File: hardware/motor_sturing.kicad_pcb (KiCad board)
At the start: 4 copper layers, 160 x 100 mm, 330 parts, among them CON1 BARREL_JACK, J1 DB25_STACKED, J2 ETHERNET_DUAL, M1 NMOS, M10 NMOS, M11 NMOS, M12 NMOS, M2 NMOS, M3 NMOS, M4 NMOS, M5 NMOS, M6 NMOS, M7 NMOS, M8 NMOS, M9 NMOS, P1 CONN_01X03, P11 CONN_01X01, P12 CONN_01X01, P13 CONN_01X01, P14 CONN_01X01, P15 CONN_01X01, P16 CONN_01X01, P17 CONN_01X01, P18 CONN_01X01, P19 CONN_01X01, P2 CONN_01X03, P20 CONN_01X01, P21 CONN_01X01, P22 CONN_01X01, P23 CONN_01X01, P24 CONN_01X01, P25 CONN_01X01, P3 CONN_01X03, P4 CONN_01X03, P5 CONN_02X07, P6 CONN_01X01, P7 CONN_01X01, P8 CONN_01X01, U1 LTC2351-14, U10 MAX3463, U11 MAX3463, U12 MAX3463, U13 MAX3463, U14 MAX3463, U15 ADuM3223BRZ, U16 TS321, U17 ACS758, U18 ADuM3223BRZ, U19 AD8226, U2 XC6SLXN-TQG144, U20 AD8226, U21 AD8226, U22 LTC2351-14, U23 LT3010, U24 ACS758, U25 AMC1204, U26 OKR_T3, U27 ADuM3223BRZ, U28 ACS758, U29 MAX3463, U3 W25Q80DV, U30 MAX3463, U31 MAX3463, U32 MAX3463, U33 MAX3463, U34 ADuM3223BRZ, U35 ACS758, U36 ADuM3223BRZ, U37 TS321, U38 AD8226, U39 AD8226, U4 KSZ9031RNXCA, U40 AD8226, U41 OKR_T3, U42 LT3010, U43 ACS758, U44 AMC1204, U45 OKR_T3, U46 TS321, U47 TS321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

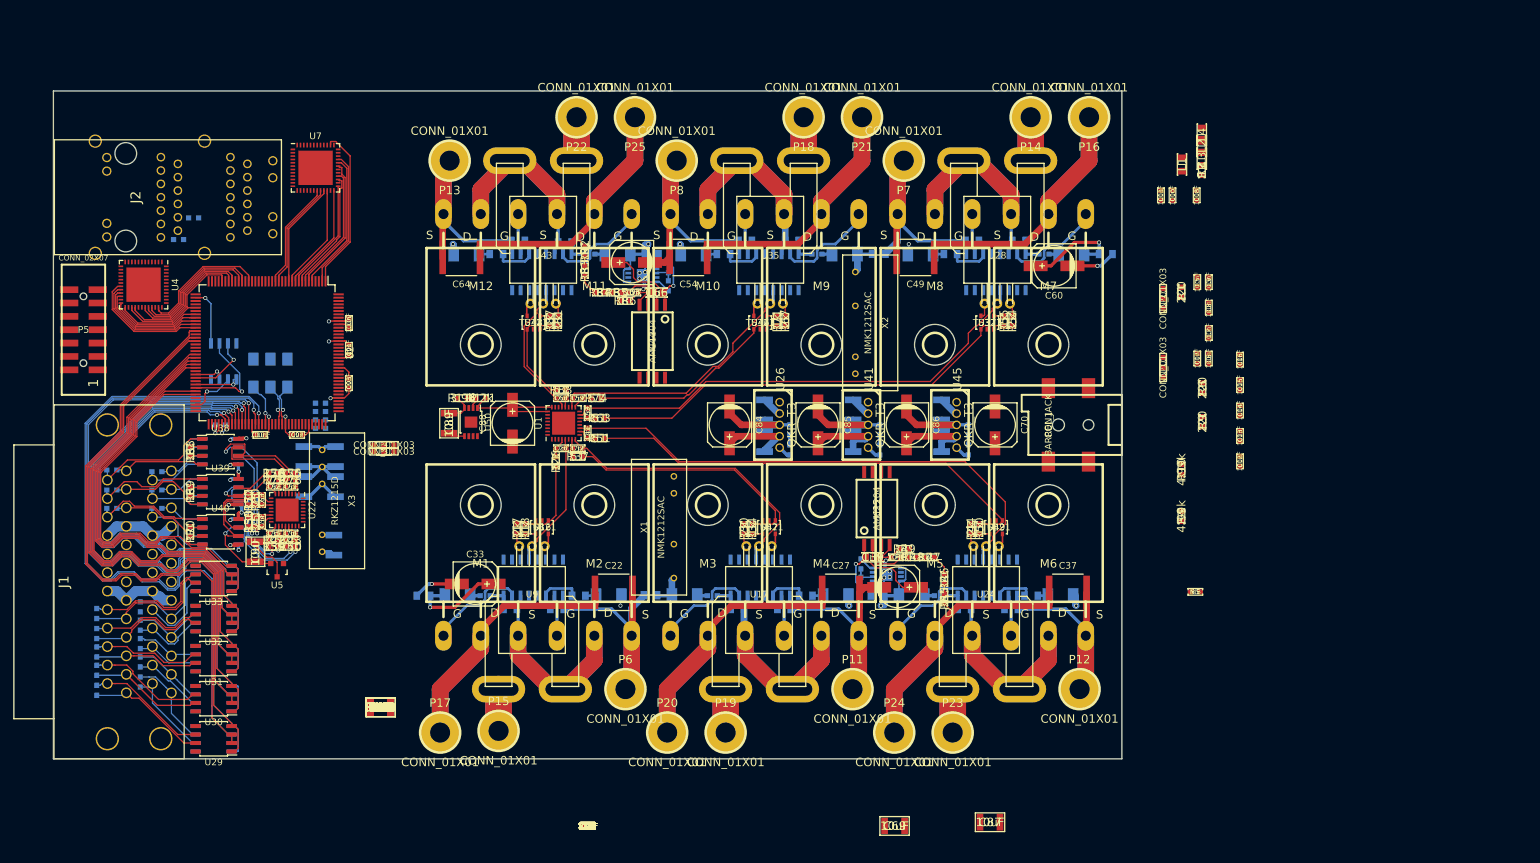
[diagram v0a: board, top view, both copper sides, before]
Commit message: Backup, clearing bottom of power section.
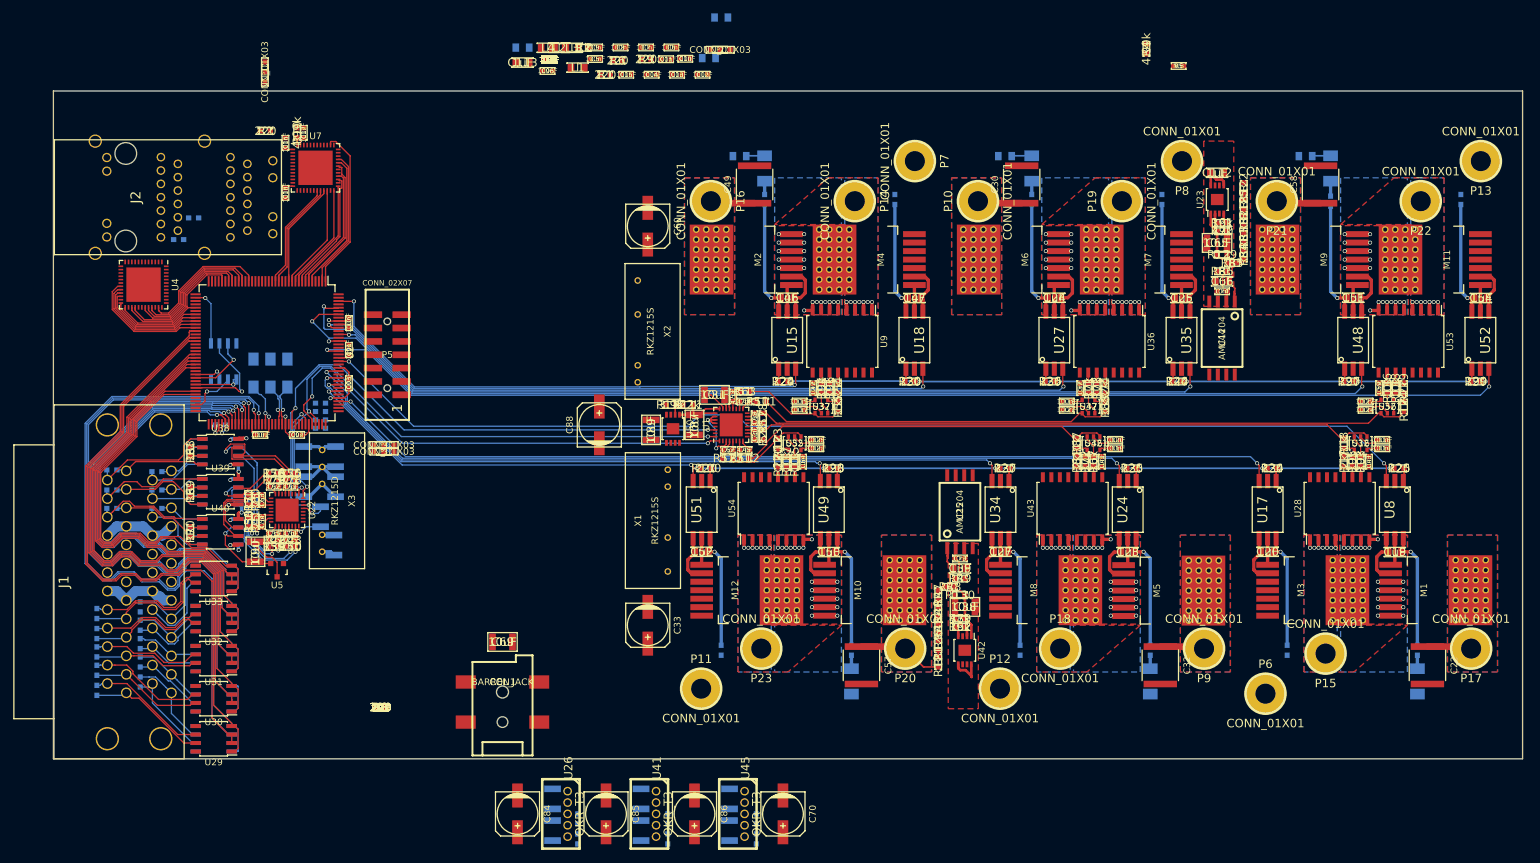
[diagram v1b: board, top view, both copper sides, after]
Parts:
- removed D11, D12, D2, D5, D6, D8: S1M, 00_Passives:DO-214AC(SMA)
- removed P24, P25: CONN_01X01, 00_Passives:conn_01x01_3mm
- added C112: 1uF, 00_Local:C0805, F.Cu at (204.2, 62.2)
- added C113: 1uF, 00_Local:C0805, F.Cu at (100.2, 45.8)
- added C114: 100nF, 00_Passives:C0603, F.Cu at (229.0, 103.5)
- added C115: 100nF, 00_Passives:C0603, F.Cu at (141.8, 96.5)
- added C116: 100nF, 00_Passives:C0603, F.Cu at (229.0, 102.2)
- added C117: 100nF, 00_Passives:C0603, F.Cu at (141.8, 97.8)
- added C118: 100nF, 00_Passives:C0603, F.Cu at (181.8, 96.5)
- added C119: 100nF, 00_Passives:C0603, F.Cu at (189.0, 103.5)
- added C120: 100nF, 00_Passives:C0603, F.Cu at (189.0, 102.2)
- added C121: 100nF, 00_Passives:C0603, F.Cu at (181.8, 97.8)
- added C122: 100nF, 00_Passives:C0603, F.Cu at (226.5, 96.5)
- added C123: 100nF, 00_Passives:C0603, F.Cu at (144.2, 103.5)
- added C124: 100nF, 00_Passives:C0603, F.Cu at (226.5, 97.8)
- added C125: 100nF, 00_Passives:C0603, F.Cu at (144.2, 102.2)
- added P10: CONN_01X01, 00_Passives:conn_01x01_3mm, F.Cu at (168.4, 66.5)
- added P9: CONN_01X01, 00_Passives:conn_01x01_3mm, F.Cu at (202.3, 133.5)
- added R113: 22, 00_Local:R0603, B.Cu at (130.0, 133.8)
- added R114: 22, 00_Local:R0603, B.Cu at (240.8, 66.3)
- added R115: 10k, 00_Passives:R0603, F.Cu at (141.0, 105.5)
- added R116: 10k, 00_Passives:R0603, F.Cu at (229.8, 94.5)
- added R117: 10k, 00_Passives:R0603, F.Cu at (139.8, 105.5)
- added R118: 10k, 00_Passives:R0603, F.Cu at (231.0, 94.5)
- added R119: 2k, 00_Local:R0603, F.Cu at (232.2, 94.5)
- added R120: 2k, 00_Local:R0603, F.Cu at (138.5, 105.5)
- added R121: R, 00_Local:R0603, F.Cu at (162.5, 135.5)
- added R122: R, 00_Local:R0603, F.Cu at (208.2, 64.5)
- added R123: 1k, 00_Local:R0603, F.Cu at (138.5, 102.8)
- added R124: 1k, 00_Local:R0603, F.Cu at (232.2, 97.2)
- added R125: R, 00_Local:R0603, F.Cu at (208.2, 67.0)
- added R126: R, 00_Local:R0603, F.Cu at (162.5, 133.0)
- added R127: 51, 00_Local:R0603, F.Cu at (131.0, 105.0)
- added R128: 51, 00_Local:R0603, F.Cu at (136.2, 99.0)
- added R129: 0.1, 00_Local:R0603, F.Cu at (205.0, 74.5)
- added R130: 0.1, 00_Local:R0603, F.Cu at (165.8, 125.5)
- added U51: Si8261BCD-C-IS, 00_Passives:SOIC-6_6.8x4.6mm_Pitch1.27mm, F.Cu at (127.1, 112.7)
- added U52: Si8261BCD-C-IS, 00_Passives:SOIC-6_6.8x4.6mm_Pitch1.27mm, F.Cu at (243.7, 87.3)
- added U53: ACS722KMATR-20AB-T, Housings_SOIC:SOIC-16_7.5x10.3mm_Pitch1.27mm, F.Cu at (232.9, 87.5)
- added U54: ACS722KMATR-20AB-T, Housings_SOIC:SOIC-16_7.5x10.3mm_Pitch1.27mm, F.Cu at (137.9, 112.5)
- added U55: TS321, 00_Passives:SOT23_5, F.Cu at (141.0, 102.7)
- added U56: TS321, 00_Passives:SOT23_5, F.Cu at (229.8, 97.2)
- C19, C20, C23, C24, C25, C46, C47, C50, C51, C52, R89, R90, R91, R92, U23, U42: moved to F.Cu
- C27, C54: value 1uF/630V -> 1uF; footprint Capacitors_SMD:C_2220 -> 00_Local:C0805
- C30, C57: value 1uF -> 1uF/630V; footprint 00_Local:C0805 -> Capacitors_SMD:C_2220; moved to F.Cu
- C32: value 47pF -> 1uF/630V; footprint 00_Local:C0603 -> Capacitors_SMD:C_2220
- C37, C64: value 1uF/630V -> 10nF; footprint Capacitors_SMD:C_2220 -> 00_Passives:C0603
- C38, C65: value 100uF/16V -> 10uF; footprint Capacitors_SMD:c_elec_6.3x5.3 -> 00_Passives:C1210
- C40: moved to B.Cu
- C41, C59: value 47pF -> 10nF; footprint 00_Local:C0603 -> 00_Passives:C0603
- C44, C45, C67: value 10nF -> 47pF; footprint 00_Passives:C0603 -> 00_Local:C0603
- C58: value 10nF -> 1uF/630V; footprint 00_Passives:C0603 -> Capacitors_SMD:C_2220
- M1, M10, M11, M12, M2, M3, M4, M5, M6, M7, M8, M9: value NMOS -> C3M0280090J; footprint 00_Passives:TO-247_GDS_below_board -> 00_Passives:TO-263-7-GDSKS
- R100, R97, R98, R99: value 10k -> 220
- R101, R102: value 10k -> 51; footprint 00_Passives:R0603 -> 00_Local:R0603
- R103, R104: value 10k -> 22; footprint 00_Passives:R0603 -> 00_Local:R0603; moved to B.Cu
- R16, R53, R62: footprint 00_Local:R0805 -> 00_Local:R0603
- R24, R35: value 22 -> 220; footprint 00_Local:R0603 -> 00_Passives:R0603; moved to F.Cu
- R25, R36: value 22 -> 220; footprint 00_Local:R0805 -> 00_Passives:R0603; moved to F.Cu
- R30, R44: value 2k -> 220; footprint 00_Local:R0603 -> 00_Passives:R0603
- R34: value 1k -> 220; footprint 00_Local:R0603 -> 00_Passives:R0603
- R37: value 51 -> 220; footprint 00_Local:R0603 -> 00_Passives:R0603
- R50: value 1k -> 22; moved to B.Cu
- R51: value 51 -> 22; moved to B.Cu
- R67: value 2k -> 10k; footprint 00_Local:R0603 -> 00_Passives:R0603
- R71: value 1k -> 10k; footprint 00_Local:R0603 -> 00_Passives:R0603
- R72: value 22 -> 10k; footprint 00_Local:R0603 -> 00_Passives:R0603; moved to F.Cu
- R73: value 22 -> 10k; footprint 00_Local:R0805 -> 00_Passives:R0603; moved to F.Cu
- R74: value 51 -> 2k
- R88: value 51 -> 1k
- U15, U18, U27, U34, U8: value ADuM3223BRZ -> Si8261BCD-C-IS; footprint Housings_SOIC:SOIC-16_3.9x9.9mm_Pitch1.27mm -> 00_Passives:SOIC-6_6.8x4.6mm_Pitch1.27mm; moved to F.Cu
- U17, U24, U35: value ACS758 -> Si8261BCD-C-IS; footprint 00_Passives:acs758 -> 00_Passives:SOIC-6_6.8x4.6mm_Pitch1.27mm
- U28, U43, U9: value ACS758 -> ACS722KMATR-20AB-T; footprint 00_Passives:acs758 -> Housings_SOIC:SOIC-16_7.5x10.3mm_Pitch1.27mm
- U36: value ADuM3223BRZ -> ACS722KMATR-20AB-T; footprint Housings_SOIC:SOIC-16_3.9x9.9mm_Pitch1.27mm -> Housings_SOIC:SOIC-16_7.5x10.3mm_Pitch1.27mm; moved to F.Cu
- U48, U49: value TS321 -> Si8261BCD-C-IS; footprint 00_Passives:SOT23_5 -> 00_Passives:SOIC-6_6.8x4.6mm_Pitch1.27mm
- X1, X2: value NMK1212SAC -> RKZ1215S
- moved R99 171.1 mm to (243.0, 93.5)
- moved R104 161.2 mm to (221.2, 66.5), turned to 90 degrees
- moved C58 161.1 mm to (219.8, 64.0), turned to 90 degrees
- moved P17 154.9 mm to (242.3, 133.5), turned to 180 degrees
- moved P13 154.4 mm to (243.8, 60.5)
- moved R97 153.0 mm to (224.0, 93.5)
- moved C43 152.5 mm to (227.0, 105.5), turned to 270 degrees
- moved R93 151.3 mm to (225.8, 105.5), turned to 90 degrees
- moved R95 150.1 mm to (224.5, 105.5), turned to 270 degrees
- moved C16 146.6 mm to (64.8, 57.7)
- moved D1 144.3 mm to (234.2, 138.4), turned to 90 degrees
- moved R10 141.7 mm to (66.5, 56.2)
- moved P1 141.6 mm to (61.7, 47.2)
- moved R15 139.8 mm to (234.2, 133.7), turned to 270 degrees
- moved C17 138.0 mm to (67.5, 56.2)
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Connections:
- net Net-(C22-Pad1) renamed /Drive_1/HV0
- net Net-(U2-Pad97) renamed /FPGA/HB_DISABLE
- C20 pad 2: /Drive_1/BRIDGE- -> Net-(C20-Pad2)
- C21 pad 1: /Drive_1/ISOL_12V -> /Drive_1/ISOL_15V
- C23 pad 1: /Drive_1/ISOL_12V -> Net-(C23-Pad1)
- C23 pad 2: /Drive_1/BRIDGE- -> Net-(C23-Pad2)
- C25 pad 2: /Drive_1/BRIDGE- -> Net-(C25-Pad2)
- C27 pad 2: /Drive_1/BRIDGE- -> Net-(C27-Pad2)
- C28 pad 1: /Drive_1/ISOL_12V -> /Drive_1/ISOL_15V
- C29 pad 1: Net-(C29-Pad1) -> /Drive_2/ISOL_15V
- C29 pad 2: Net-(C29-Pad2) -> /Drive_2/BRIDGE-
- C30 pad 1: Net-(C30-Pad1) -> /Drive_2/HV1
- C30 pad 2: /Drive_1/BRIDGE- -> /Drive_2/BRIDGE-
- C32 pad 1: /Drive_1/CUR1 -> /Drive_1/HV1
- C32 pad 2: GND -> /Drive_1/BRIDGE-
- C33 pad 1: /Drive_1/ISOL_12V -> /Drive_1/ISOL_15V
- C37 pad 2: /Drive_1/BRIDGE- -> GND
- C38 pad 1: /Drive_1/ISOL_5V -> Net-(C38-Pad1)
- C41 pad 1: /Drive_1/CUR2 -> Net-(C41-Pad1)
- C44 pad 1: Net-(C44-Pad1) -> /Drive_2/CUR1
- C45 pad 1: Net-(C45-Pad1) -> /Drive_1/CUR1
- C47 pad 2: /Drive_2/BRIDGE- -> Net-(C47-Pad2)
- C48 pad 1: /Drive_2/ISOL_12V -> /Drive_2/ISOL_15V
- C49 pad 1: Net-(C49-Pad1) -> /Drive_2/HV0
- C50 pad 1: /Drive_2/ISOL_12V -> Net-(C50-Pad1)
- C50 pad 2: /Drive_2/BRIDGE- -> Net-(C50-Pad2)
- C52 pad 2: /Drive_2/BRIDGE- -> Net-(C52-Pad2)
- C54 pad 2: /Drive_2/BRIDGE- -> Net-(C54-Pad2)
- C55 pad 1: /Drive_2/ISOL_12V -> /Drive_2/ISOL_15V
- C56 pad 1: Net-(C56-Pad1) -> /Drive_1/ISOL_15V
- C56 pad 2: Net-(C56-Pad2) -> /Drive_1/BRIDGE-
- C57 pad 1: Net-(C57-Pad1) -> /Drive_1/HV2
- C57 pad 2: /Drive_2/BRIDGE- -> /Drive_1/BRIDGE-
- C58 pad 1: Net-(C58-Pad1) -> /Drive_2/HV2
- C58 pad 2: GND -> /Drive_2/BRIDGE-
- C59 pad 1: /Drive_2/CUR1 -> Net-(C59-Pad1)
- C60 pad 1: /Drive_2/ISOL_12V -> /Drive_2/ISOL_15V
- C64 pad 2: /Drive_2/BRIDGE- -> GND
- C65 pad 1: /Drive_2/ISOL_5V -> Net-(C65-Pad1)
- C67 pad 1: Net-(C67-Pad1) -> /Drive_1/CUR2
- D1 pad A: /Drive_1/ISOL_12V -> /Drive_1/ISOL_15V
- D10 pad A: /Drive_2/ISOL_12V -> /Drive_1/ISOL_15V
- D3 pad A: /Drive_1/ISOL_12V -> /Drive_2/ISOL_15V
- D4 pad A: /Drive_1/ISOL_12V -> /Drive_1/ISOL_15V
- D7 pad A: /Drive_2/ISOL_12V -> /Drive_2/ISOL_15V
- D9 pad A: /Drive_2/ISOL_12V -> /Drive_2/ISOL_15V
- M1 pad S: Net-(C19-Pad2) -> /Drive_1/HB0
- M10 pad D: Net-(C51-Pad2) -> /Drive_1/HV2
- M10 pad S: /Drive_2/BRIDGE- -> /Drive_1/HB2
- M11 pad D: Net-(C64-Pad1) -> /Drive_2/HB2
- M11 pad S: Net-(C56-Pad2) -> /Drive_2/BRIDGE-
- M12 pad D: Net-(C56-Pad2) -> /Drive_1/HB2
- M12 pad S: /Drive_2/BRIDGE- -> /Drive_1/BRIDGE-
- M2 pad D: Net-(C19-Pad2) -> /Drive_2/HV0
- M2 pad S: /Drive_1/BRIDGE- -> /Drive_2/HB0
- M3 pad D: Net-(C27-Pad1) -> /Drive_1/HB0
- M3 pad S: Net-(C24-Pad2) -> /Drive_1/BRIDGE-
- M4 pad D: Net-(C24-Pad2) -> /Drive_2/HB0
- M4 pad S: /Drive_1/BRIDGE- -> /Drive_2/BRIDGE-
- M5 pad D: Net-(C37-Pad1) -> /Drive_1/HV1
- M5 pad S: Net-(C29-Pad2) -> /Drive_1/HB1
- M6 pad D: Net-(C29-Pad2) -> /Drive_2/HV1
- M6 pad S: /Drive_1/BRIDGE- -> /Drive_2/HB1
- M7 pad D: Net-(C49-Pad1) -> /Drive_2/HB1
- M7 pad S: Net-(C46-Pad2) -> /Drive_2/BRIDGE-
- M8 pad D: Net-(C46-Pad2) -> /Drive_1/HB1
- M8 pad S: /Drive_2/BRIDGE- -> /Drive_1/BRIDGE-
- M9 pad D: Net-(C54-Pad1) -> /Drive_2/HV2
- M9 pad S: Net-(C51-Pad2) -> /Drive_2/HB2
- P14 pad 1: Net-(P14-Pad1) -> /Drive_2/OUT0
- P15 pad 1: Net-(P15-Pad1) -> /Drive_1/OUT0
- P16 pad 1: Net-(C49-Pad1) -> /Drive_2/HV0
- P18 pad 1: Net-(P18-Pad1) -> /Drive_1/OUT1
- P19 pad 1: Net-(P19-Pad1) -> /Drive_2/OUT1
- P20 pad 1: Net-(C27-Pad1) -> /Drive_1/HV2
- P21 pad 1: Net-(C54-Pad1) -> /Drive_2/HV2
- P22 pad 1: Net-(P22-Pad1) -> /Drive_2/OUT2
- P23 pad 1: Net-(P23-Pad1) -> /Drive_1/OUT2
- R100 pad 1: Net-(C45-Pad1) -> Net-(R100-Pad1)
- R100 pad 2: GND -> +3.3V
- R101 pad 1: +5V -> /Drive_2/CUR1
- R101 pad 2: Net-(C58-Pad1) -> Net-(R101-Pad2)
- R102 pad 1: +5V -> /Drive_1/CUR1
- R102 pad 2: Net-(C67-Pad1) -> Net-(R102-Pad2)
- R103 pad 1: Net-(C58-Pad1) -> Net-(C50-Pad1)
- R103 pad 2: GND -> Net-(D10-PadC)
- R104 pad 1: Net-(C67-Pad1) -> Net-(C51-Pad1)
- R104 pad 2: GND -> Net-(D9-PadC)
- R16 pad 2: Net-(D2-PadC) -> /Drive_1/ISOL_15V
- R24 pad 1: Net-(C24-Pad1) -> Net-(R24-Pad1)
- R24 pad 2: Net-(D3-PadC) -> +3.3V
- R25 pad 1: Net-(C25-Pad1) -> Net-(R25-Pad1)
- R25 pad 2: Net-(D4-PadC) -> +3.3V
- R30 pad 2: Net-(R30-Pad2) -> +3.3V
- R34 pad 2: Net-(R30-Pad1) -> +3.3V
- R35 pad 1: Net-(C29-Pad1) -> Net-(R35-Pad1)
- R35 pad 2: Net-(D5-PadC) -> +3.3V
- R36 pad 1: Net-(C30-Pad1) -> Net-(R36-Pad1)
- R36 pad 2: Net-(D6-PadC) -> +3.3V
- R37 pad 1: /Drive_1/CUR1 -> Net-(R37-Pad1)
- R37 pad 2: Net-(R34-Pad1) -> +3.3V
- R44 pad 2: Net-(R44-Pad2) -> +3.3V
- R45 pad 1: Net-(C37-Pad1) -> Net-(R126-Pad2)
- R50 pad 1: Net-(R50-Pad1) -> Net-(C23-Pad1)
- R50 pad 2: Net-(R44-Pad1) -> Net-(D4-PadC)
- R51 pad 1: /Drive_1/CUR2 -> Net-(C24-Pad1)
- R51 pad 2: Net-(R50-Pad1) -> Net-(D3-PadC)
- R53 pad 2: Net-(D8-PadC) -> /Drive_2/ISOL_15V
- R61 pad 1: Net-(C51-Pad1) -> Net-(C27-Pad1)
- R61 pad 2: Net-(D9-PadC) -> /Drive_1/ISOL_15V
- R62 pad 1: Net-(C52-Pad1) -> Net-(C25-Pad1)
- R62 pad 2: Net-(D10-PadC) -> /Drive_2/ISOL_15V
- R67 pad 1: Net-(R67-Pad1) -> +3V3
- R67 pad 2: Net-(R67-Pad2) -> Net-(C41-Pad1)
- R71 pad 1: Net-(R71-Pad1) -> +3V3
- R71 pad 2: Net-(R67-Pad1) -> Net-(C37-Pad1)
- R72 pad 1: Net-(C56-Pad1) -> Net-(C41-Pad1)
- R72 pad 2: Net-(D11-PadC) -> GND
- R73 pad 1: Net-(C57-Pad1) -> Net-(C37-Pad1)
- R73 pad 2: Net-(D12-PadC) -> GND
- R74 pad 1: /Drive_2/CUR1 -> Net-(R74-Pad1)
- R74 pad 2: Net-(R71-Pad1) -> Net-(R74-Pad2)
- R82 pad 1: Net-(C64-Pad1) -> Net-(R125-Pad2)
- R87 pad 1: Net-(R87-Pad1) -> Net-(R102-Pad2)
- R88 pad 1: /Drive_2/CUR2 -> Net-(R101-Pad2)
- R88 pad 2: Net-(R87-Pad1) -> Net-(R74-Pad1)
- R93 pad 1: +5V -> +3V3
- R94 pad 1: +5V -> +3V3
- R97 pad 1: +5V -> Net-(R97-Pad1)
- R97 pad 2: Net-(C45-Pad1) -> +3.3V
- R98 pad 1: +5V -> Net-(R98-Pad1)
- R98 pad 2: Net-(C44-Pad1) -> +3.3V
- R99 pad 1: Net-(C44-Pad1) -> Net-(R99-Pad1)
- R99 pad 2: GND -> +3.3V
- U1 pad 10: /Drive_1/CUR2 -> /Drive_1/CUR0
- U1 pad 14: /Drive_2/CUR0 -> /Drive_2/CUR2
- U1 pad 20: /Drive_2/CUR2 -> /Drive_2/CUR0
- U1 pad 4: /Drive_1/CUR0 -> /Drive_1/CUR2
- U15 pad 1: /Drive_1/H1 -> Net-(R24-Pad1)
- U15 pad 2: /FPGA/HB_L1 -> (no net)
- U15 pad 3: +3.3V -> /Drive_2/H0
- U15 pad 4: GND -> Net-(C46-Pad2)
- U15 pad 5: /Drive_1/DISABLE -> Net-(M2-PadG)
- U15 pad 6: (no net) -> Net-(C46-Pad1)
- U17 pad 1: +5V -> Net-(R34-Pad1)
- U17 pad 2: GND -> (no net)
- U17 pad 3: Net-(R30-Pad2) -> /FPGA/HB_L0
- U17 pad 4: Net-(P19-Pad1) -> Net-(C20-Pad2)
- U17 pad 5: Net-(C24-Pad2) -> Net-(M3-PadG)
- U18 pad 1: /Drive_1/H2 -> Net-(R30-Pad1)
- U18 pad 2: /FPGA/HB_L2 -> (no net)
- U18 pad 3: +3.3V -> /FPGA/HB_L3
- U18 pad 4: GND -> Net-(C47-Pad2)
- U18 pad 5: /Drive_1/DISABLE -> Net-(M4-PadG)
- U18 pad 6: (no net) -> Net-(C47-Pad1)
- U2 pad 100: Net-(U2-Pad100) -> /FPGA/VOLTAGE_D0
- U2 pad 101: Net-(U2-Pad101) -> /Drive_1/VOLTAGE_CLOCK
- U2 pad 102: Net-(U2-Pad102) -> /FPGA/SD1
- U2 pad 104: Net-(U2-Pad104) -> /FPGA/SD0
- U2 pad 105: Net-(U2-Pad105) -> /FPGA/SCK
- U2 pad 112: Net-(U2-Pad112) -> /FPGA/HB_L0
- U2 pad 115: Net-(U2-Pad115) -> /FPGA/HB_L2
- U2 pad 117: Net-(U2-Pad117) -> /FPGA/HB_L1
- U2 pad 119: Net-(U2-Pad119) -> /Drive_1/H2
- U2 pad 121: Net-(U2-Pad121) -> /Drive_1/H1
- U2 pad 124: Net-(U2-Pad124) -> /Drive_1/H0
- U2 pad 23: Net-(U2-Pad23) -> /FPGA/ETH_RESET(0)
- U2 pad 98: Net-(U2-Pad98) -> /FPGA/CONV
- U2 pad 99: Net-(U2-Pad99) -> /FPGA/VOLTAGE_D1
- U23 pad 5: /Drive_2/ISOL_12V -> /Drive_2/ISOL_15V
- U23 pad 8: /Drive_2/ISOL_12V -> /Drive_2/ISOL_15V
- U24 pad 1: +5V -> Net-(R35-Pad1)
- U24 pad 2: GND -> (no net)
- U24 pad 3: Net-(R44-Pad2) -> /Drive_1/H1
- U24 pad 4: Net-(P23-Pad1) -> Net-(C23-Pad2)
- U24 pad 5: Net-(C29-Pad2) -> Net-(M5-PadG)
- U27 pad 1: /Drive_2/H0 -> Net-(R36-Pad1)
- U27 pad 2: /FPGA/HB_L3 -> (no net)
- U27 pad 3: +3.3V -> /Drive_2/H1
- U27 pad 4: GND -> Net-(C24-Pad2)
- U27 pad 5: /Drive_1/DISABLE -> Net-(M6-PadG)
- U27 pad 6: (no net) -> Net-(C24-Pad1)
- U28 pad 1: +5V -> /Drive_1/OUT0
- U28 pad 2: GND -> /Drive_1/OUT0
- U28 pad 3: Net-(R54-Pad2) -> /Drive_1/OUT0
- U28 pad 4: Net-(P14-Pad1) -> /Drive_1/OUT0
- U28 pad 5: Net-(C46-Pad2) -> /Drive_1/HB0
- U34 pad 1: /Drive_2/H1 -> Net-(R37-Pad1)
- U34 pad 2: /FPGA/HB_L4 -> (no net)
- U34 pad 3: +3.3V -> /FPGA/HB_L1
- U34 pad 4: GND -> Net-(C27-Pad2)
- U34 pad 5: /Drive_1/DISABLE -> Net-(M8-PadG)
- U34 pad 6: (no net) -> Net-(C27-Pad1)
- U35 pad 1: +5V -> Net-(R44-Pad1)
- U35 pad 2: GND -> (no net)
- U35 pad 3: Net-(R67-Pad2) -> /FPGA/HB_L4
- U35 pad 4: Net-(P18-Pad1) -> Net-(C25-Pad2)
- U35 pad 5: Net-(C51-Pad2) -> Net-(M7-PadG)
- U36 pad 1: /Drive_2/H2 -> /Drive_2/OUT1
- U36 pad 10: Net-(M12-PadG) -> +3V3
- U36 pad 11: Net-(C57-Pad1) -> GND
- U36 pad 12: (no net) -> Net-(R74-Pad2)
- U36 pad 13: (no net) -> GND
- U36 pad 14: Net-(C56-Pad2) -> GND
- U36 pad 15: Net-(M11-PadG) -> GND
- U36 pad 16: Net-(C56-Pad1) -> (no net)
- U36 pad 2: /FPGA/HB_L5 -> /Drive_2/OUT1
- U36 pad 3: +3.3V -> /Drive_2/OUT1
- U36 pad 4: GND -> /Drive_2/OUT1
- U36 pad 5: /Drive_1/DISABLE -> /Drive_2/HB1
- U36 pad 6: (no net) -> /Drive_2/HB1
- U36 pad 7: (no net) -> /Drive_2/HB1
- U36 pad 8: +3.3V -> /Drive_2/HB1
- U36 pad 9: /Drive_2/BRIDGE- -> (no net)
- U42 pad 5: /Drive_1/ISOL_12V -> /Drive_1/ISOL_15V
- U42 pad 8: /Drive_1/ISOL_12V -> /Drive_1/ISOL_15V
- U43 pad 1: +5V -> /Drive_1/OUT1
- U43 pad 2: GND -> /Drive_1/OUT1
- U43 pad 3: Net-(R81-Pad2) -> /Drive_1/OUT1
- U43 pad 4: Net-(P22-Pad1) -> /Drive_1/OUT1
- U43 pad 5: Net-(C56-Pad2) -> /Drive_1/HB1
- U46 pad 1: Net-(R71-Pad1) -> Net-(R102-Pad2)
- U46 pad 3: Net-(C45-Pad1) -> Net-(C41-Pad1)
- U46 pad 4: Net-(R67-Pad1) -> Net-(R81-Pad1)
- U47 pad 1: Net-(R34-Pad1) -> Net-(R101-Pad2)
- U47 pad 3: Net-(C44-Pad1) -> Net-(C37-Pad1)
- U47 pad 4: Net-(R30-Pad1) -> Net-(R74-Pad1)
- U48 pad 1: Net-(R87-Pad1) -> Net-(R97-Pad1)
- U48 pad 2: -5V -> (no net)
- U48 pad 3: Net-(C67-Pad1) -> /Drive_2/H2
- U48 pad 4: Net-(R81-Pad1) -> Net-(C51-Pad2)
- U48 pad 5: +5V -> Net-(M9-PadG)
- U49 pad 1: Net-(R50-Pad1) -> Net-(R98-Pad1)
- U49 pad 2: -5V -> (no net)
- U49 pad 3: Net-(C58-Pad1) -> /Drive_1/H2
- U49 pad 4: Net-(R44-Pad1) -> Net-(C50-Pad2)
- U49 pad 5: +5V -> Net-(M10-PadG)
- U8 pad 1: /Drive_1/H0 -> Net-(R25-Pad1)
- U8 pad 2: /FPGA/HB_L0 -> (no net)
- U8 pad 3: +3.3V -> /Drive_1/H0
- U8 pad 4: GND -> Net-(C19-Pad2)
- U8 pad 5: /Drive_1/DISABLE -> Net-(M1-PadG)
- U8 pad 6: (no net) -> Net-(C19-Pad1)
- U9 pad 1: +5V -> /Drive_2/OUT0
- U9 pad 2: GND -> /Drive_2/OUT0
- U9 pad 3: Net-(R17-Pad2) -> /Drive_2/OUT0
- U9 pad 4: Net-(P15-Pad1) -> /Drive_2/OUT0
- U9 pad 5: Net-(C19-Pad2) -> /Drive_2/HB0
- X1 pad 7: /Drive_1/ISOL_12V -> /Drive_1/ISOL_15V
- X2 pad 7: /Drive_2/ISOL_12V -> /Drive_2/ISOL_15V
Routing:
- net /Drive_2/BRIDGE-: track 360.9 -> 1.60 mm, vias 6 -> 0
- net /Drive_1/BRIDGE-: track 360.9 -> 1.60 mm, vias 6 -> 0
- net GND: track 391.8 -> 87.2 mm, vias 6 -> 7
- net +3.3V: track 13.2 -> 229.1 mm, vias 1 -> 13
- net /FPGA/HB_L5: track 0.00 -> 181.8 mm, vias 0 -> 2
- net /Drive_2/H2: track 0.00 -> 169.3 mm, vias 0 -> 2
- net /Drive_1/H0: track 0.00 -> 167.4 mm, vias 0 -> 2
- net /FPGA/HB_L0: track 0.00 -> 144.2 mm, vias 0 -> 2
- net /Drive_2/ISOL_12V: track 140.4 -> 0.00 mm, vias 5 -> 0
- net /Drive_1/ISOL_12V: track 140.4 -> 0.00 mm, vias 5 -> 0
- net /FPGA/HB_L4: track 0.00 -> 134.1 mm, vias 0 -> 2
- net /Drive_1/H1: track 0.00 -> 129.6 mm, vias 0 -> 2
- net /Drive_2/H1: track 0.00 -> 123.2 mm, vias 0 -> 2
- net /FPGA/HB_L1: track 0.00 -> 108.6 mm, vias 0 -> 2
- net Net-(R124-Pad1): track 0.00 -> 97.9 mm
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- added copper zone on F.Cu, net /Drive_1/BRIDGE-
- added copper zone on B.Cu, net /Drive_1/HB0
- added copper zone on F.Cu, net /Drive_1/HB0
- added copper zone on In1.Cu, net /Drive_1/HB0
- added copper zone on In2.Cu, net /Drive_1/HB0
- added copper zone on B.Cu, net /Drive_1/HB1
- added copper zone on F.Cu, net /Drive_1/HB1
- added copper zone on In1.Cu, net /Drive_1/HB1
- added copper zone on In2.Cu, net /Drive_1/HB1
- added copper zone on B.Cu, net /Drive_1/HB2
- added copper zone on F.Cu, net /Drive_1/HB2
- added copper zone on In1.Cu, net /Drive_1/HB2
- added copper zone on In2.Cu, net /Drive_1/HB2
- added copper zone on B.Cu, net /Drive_1/HV0
- added copper zone on F.Cu, net /Drive_1/HV0
- added copper zone on In1.Cu, net /Drive_1/HV0
- added copper zone on In2.Cu, net /Drive_1/HV0
- added copper zone on B.Cu, net /Drive_1/HV1
- added copper zone on F.Cu, net /Drive_1/HV1
- added copper zone on In1.Cu, net /Drive_1/HV1
- added copper zone on In2.Cu, net /Drive_1/HV1
- added copper zone on B.Cu, net /Drive_1/HV2
- added copper zone on F.Cu, net /Drive_1/HV2
- added copper zone on In1.Cu, net /Drive_1/HV2
- added copper zone on In2.Cu, net /Drive_1/HV2
- added copper zone on B.Cu, net /Drive_1/OUT0
- added copper zone on F.Cu, net /Drive_1/OUT0
- added copper zone on In1.Cu, net /Drive_1/OUT0
- added copper zone on In2.Cu, net /Drive_1/OUT0
- added copper zone on B.Cu, net /Drive_1/OUT1
- added copper zone on F.Cu, net /Drive_1/OUT1
- added copper zone on In1.Cu, net /Drive_1/OUT1
- added copper zone on In2.Cu, net /Drive_1/OUT1
- added copper zone on B.Cu, net /Drive_1/OUT2
- added copper zone on F.Cu, net /Drive_1/OUT2
- added copper zone on In1.Cu, net /Drive_1/OUT2
- added copper zone on In2.Cu, net /Drive_1/OUT2
- added copper zone on F.Cu, net /Drive_2/BRIDGE-
- added copper zone on B.Cu, net /Drive_2/HB0
- added copper zone on F.Cu, net /Drive_2/HB0
- added copper zone on In1.Cu, net /Drive_2/HB0
- added copper zone on In2.Cu, net /Drive_2/HB0
- added copper zone on B.Cu, net /Drive_2/HB1
- added copper zone on F.Cu, net /Drive_2/HB1
- added copper zone on In1.Cu, net /Drive_2/HB1
- added copper zone on In2.Cu, net /Drive_2/HB1
- added copper zone on B.Cu, net /Drive_2/HB2
- added copper zone on F.Cu, net /Drive_2/HB2
- added copper zone on In1.Cu, net /Drive_2/HB2
- added copper zone on In2.Cu, net /Drive_2/HB2
- added copper zone on B.Cu, net /Drive_2/HV0
- added copper zone on F.Cu, net /Drive_2/HV0
- added copper zone on In1.Cu, net /Drive_2/HV0
- added copper zone on In2.Cu, net /Drive_2/HV0
- added copper zone on B.Cu, net /Drive_2/HV1
- added copper zone on F.Cu, net /Drive_2/HV1
- added copper zone on In1.Cu, net /Drive_2/HV1
- added copper zone on In2.Cu, net /Drive_2/HV1
- added copper zone on B.Cu, net /Drive_2/HV2
- added copper zone on F.Cu, net /Drive_2/HV2
- added copper zone on In1.Cu, net /Drive_2/HV2
- added copper zone on In2.Cu, net /Drive_2/HV2
- added copper zone on B.Cu, net /Drive_2/OUT0
- added copper zone on F.Cu, net /Drive_2/OUT0
- added copper zone on In1.Cu, net /Drive_2/OUT0
- added copper zone on In2.Cu, net /Drive_2/OUT0
- added copper zone on B.Cu, net /Drive_2/OUT1
- added copper zone on F.Cu, net /Drive_2/OUT1
- added copper zone on In1.Cu, net /Drive_2/OUT1
- added copper zone on In2.Cu, net /Drive_2/OUT1
- added copper zone on B.Cu, net /Drive_2/OUT2
- added copper zone on F.Cu, net /Drive_2/OUT2
- added copper zone on In1.Cu, net /Drive_2/OUT2
- added copper zone on In2.Cu, net /Drive_2/OUT2
- removed copper zone on In1.Cu, net /Drive_1/BRIDGE-
- removed copper zone on In2.Cu, net /Drive_1/BRIDGE-
- removed copper zone on In1.Cu, net /Drive_2/BRIDGE-
- removed copper zone on In2.Cu, net /Drive_2/BRIDGE-
- removed copper zone on In1.Cu, net GND
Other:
- board size 160 x 100 mm -> 220 x 100 mm

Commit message: Progress.
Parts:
- removed CON1: BARREL_JACK, 00_Passives:smd_barrel_jack
- added C126: 100nF, 00_Passives:C0603, F.Cu at (221.0, 96.8)
- added C127: 100nF, 00_Passives:C0603, F.Cu at (216.0, 103.2)
- added C128: 100nF, 00_Passives:C0603, F.Cu at (176.2, 96.8)
- added C129: 100nF, 00_Passives:C0603, F.Cu at (176.0, 103.2)
- added C130: 100nF, 00_Passives:C0603, F.Cu at (136.2, 96.8)
- added C131: 100nF, 00_Passives:C0603, F.Cu at (131.2, 103.2)
- added D2: LED_592, 00_Passives:LED_592-3030-013F, F.Cu at (38.1, 87.5)
- added D5: DIODE, Diodes_SMD:SOD-323, B.Cu at (85.2, 67.2)
- added M13: BSS138, 00_Passives:SOT23_GSD, B.Cu at (85.0, 63.5)
- added P24: CONN_01X02, 00_Passives:FCI_02_5mm, F.Cu at (40.0, 80.0)
- added P25: CONN_01X03, Pin_Headers:Pin_Header_Straight_1x03, F.Cu at (88.0, 68.6)
- added P26: CONN_01X03, Pin_Headers:Pin_Header_Straight_1x03, F.Cu at (88.0, 58.1)
- added P27: CONN_01X02, Connect:PINHEAD1-2, F.Cu at (77.5, 122.2)
- added P28: CONN_01X02, Connect:PINHEAD1-2, F.Cu at (77.5, 128.0)
- added P29: CONN_01X02, Connect:PINHEAD1-2, F.Cu at (77.5, 133.5)
- added P30: CONN_01X02, Connect:PINHEAD1-2, F.Cu at (77.5, 139.2)
- added R131: 220, 00_Passives:R0603, F.Cu at (48.8, 89.0)
- added R132: 220, 00_Passives:R0603, F.Cu at (46.2, 89.0)
- added R133: 220, 00_Passives:R0603, F.Cu at (47.5, 89.0)
- added R134: 220, 00_Passives:R0603, F.Cu at (50.0, 89.0)
- added R135: 15k, 00_Passives:R0603, B.Cu at (38.5, 111.8)
- added R136: 15k, 00_Passives:R0603, B.Cu at (40.2, 118.8)
- added R137: 4.7k, 00_Passives:R0603, B.Cu at (38.5, 120.0)
- added R138: 4.7k, 00_Passives:R0603, B.Cu at (40.5, 113.0)
- added U57: LM75, Housings_SOIC:SOIC-8_3.9x4.9mm_Pitch1.27mm, F.Cu at (156.5, 98.5)
- added U58: ips511g, Housings_SOIC:SOIC-8_3.9x4.9mm_Pitch1.27mm, B.Cu at (33.8, 111.5)
- added U59: ips511g, Housings_SOIC:SOIC-8_3.9x4.9mm_Pitch1.27mm, B.Cu at (33.6, 120.5)
- added U60: UCN5841A, Housings_DIP:DIP-18_W7.62mm, F.Cu at (64.0, 120.9)
- added U61: DS28CM00, 00_Passives:SOT23_5, F.Cu at (91.0, 87.5)
- C1, C10, C100, C101, C102, C103, C107, C11, C110, C111, C12, C13, C14, C15, C16, C18, C2, C5, C6, C69, C7, C8, C9, C92, C94, C95, C98, C99, L1, P1, P2, P3, P4, R2, R3, R4, R8, R9: moved to B.Cu
- C105, C21, C28, C29, C48, C55, C56, D1, D10, D3, D4, D7, D9, R103, R104, R11, R113, R114, R12, R13, R14, R15, R16, R50, R51, R52, R53, R61, R62, U3, U6: moved to F.Cu
- C33: value 100uF/16V -> 100nF; footprint Capacitors_SMD:c_elec_6.3x5.3 -> 00_Passives:C0603
- C60: value 100uF/16V -> 100nF; footprint Capacitors_SMD:c_elec_6.3x5.3 -> 00_Passives:C0603; moved to B.Cu
- P10, P11, P12, P13, P14, P15, P16, P17, P18, P19, P20, P21, P22, P23, P6, P7, P8, P9: footprint 00_Passives:conn_01x01_3mm -> 00_Passives:WE_9774080151R
- X1, X2: value RKZ1215S -> R2S-1215/H; footprint 00_Passives:RKZXXXXS -> 00_Passives:RECOM_R2S
- moved C21 153.7 mm to (221.5, 138.0), turned to 0 degrees
- moved R4 145.6 mm to (51.5, 75.2), turned to 180 degrees
- moved R5 141.9 mm to (63.8, 90.8), turned to 270 degrees
- moved C28 107.1 mm to (181.5, 138.0), turned to 0 degrees
- moved C113 105.6 mm to (157.2, 134.7), turned to 180 degrees
- moved C56 99.2 mm to (136.5, 138.0), turned to 0 degrees
- moved C60 93.9 mm to (54.0, 138.0), turned to 0 degrees
- moved R8 89.4 mm to (40.8, 61.5), turned to 180 degrees
- moved C1 88.0 mm to (47.2, 60.2), turned to 90 degrees
- moved C2 84.3 mm to (47.2, 64.2), turned to 90 degrees
- moved R9 81.5 mm to (40.7, 69.0)
- moved C6 77.7 mm to (54.0, 80.0), turned to 0 degrees
- moved R3 74.9 mm to (61.2, 69.5), turned to 90 degrees
- moved C7 73.6 mm to (53.3, 77.0), turned to 270 degrees
- moved C8 71.8 mm to (54.0, 81.5), turned to 0 degrees
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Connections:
- C33 pad 1: /Drive_1/ISOL_15V -> +3.3V
- C33 pad 2: /Drive_1/BRIDGE- -> GND
- C60 pad 1: /Drive_2/ISOL_15V -> +3.3V
- C60 pad 2: /Drive_2/BRIDGE- -> GND
- C80 pad 1: +3V3 -> +3.3V
- C85 pad 1: +3V3 -> +3.3V
- J1 pad A20: +12V -> Net-(J1-PadA20)
- J1 pad A7: +12V -> Net-(J1-PadA20)
- J1 pad B20: +12V -> Net-(J1-PadB20)
- J1 pad B7: +12V -> Net-(J1-PadB20)
- J2 pad 10: /FPGA/TRXD0_P -> /FPGA/TRXC0_P
- J2 pad 11: /FPGA/TRXA0_N -> /FPGA/TRXB0_N
- J2 pad 12: Net-(C4-Pad1) -> Net-(C3-Pad1)
- J2 pad 13: /FPGA/TRXB0_P -> /FPGA/TRXA0_P
- J2 pad 2: /FPGA/TRXC0_P -> /FPGA/TRXD0_P
- J2 pad 3: /FPGA/TRXD0_N -> /FPGA/TRXC0_N
- J2 pad 4: Net-(C1-Pad1) -> Net-(C2-Pad1)
- J2 pad 5: /FPGA/TRXA0_P -> /FPGA/TRXB0_P
- J2 pad 6: /FPGA/TRXB0_N -> /FPGA/TRXA0_N
- J2 pad 7: Net-(C3-Pad1) -> Net-(C4-Pad1)
- J2 pad 8: /FPGA/TRXC0_N -> /FPGA/TRXD0_N
- J2 pad 9: Net-(C2-Pad1) -> Net-(C1-Pad1)
- R115 pad 1: +3V3 -> +3.3V
- R116 pad 1: +3V3 -> +3.3V
- R67 pad 1: +3V3 -> +3.3V
- R71 pad 1: +3V3 -> +3.3V
- R93 pad 1: +3V3 -> +3.3V
- R94 pad 1: +3V3 -> +3.3V
- U1 pad 26: +3V3 -> +3.3V
- U1 pad 27: +3V3 -> +3.3V
- U1 pad 28: +3V3 -> +3.3V
- U1 pad 3: +3V3 -> +3.3V
- U1 pad 33: (no net) -> GND
- U2 pad 102: /FPGA/SD1 -> /FPGA/SCK
- U2 pad 105: /FPGA/SCK -> /FPGA/SD1
- U2 pad 132: /FPGA/HB_L4 -> /Drive_2/H2
- U2 pad 134: /FPGA/HB_L3 -> /FPGA/HB_L4
- U2 pad 138: /Drive_2/H2 -> /Drive_2/H1
- U2 pad 140: /Drive_2/H1 -> /FPGA/HB_L3
- U2 pad 22: Net-(U2-Pad22) -> /FPGA/AUX_STR
- U2 pad 33: Net-(U2-Pad33) -> /FPGA/SCL
- U2 pad 34: Net-(U2-Pad34) -> /FPGA/SDA
- U2 pad 48: /Drive_2/ENC_DIR4 -> /Drive_1/ENC_DIR3
- U2 pad 50: /Drive_2/ENC_DATA4 -> /Drive_1/ENC_DATA0
- U2 pad 51: /Drive_2/ENC_DIR3 -> /Drive_1/ENC_DIR0
- U2 pad 55: /Drive_2/ENC_DATA3 -> /Drive_1/ENC_DATA1
- U2 pad 56: /Drive_2/ENC_DIR2 -> /Drive_1/ENC_DIR1
- U2 pad 57: /Drive_2/ENC_DATA2 -> /Drive_1/ENC_DATA2
- U2 pad 58: /Drive_2/ENC_DIR1 -> /Drive_1/ENC_DIR2
- U2 pad 59: /Drive_2/ENC_DATA1 -> /Drive_1/ENC_DATA3
- U2 pad 66: /Drive_2/ENC_DIR0 -> /Drive_1/ENC_DATA4
- U2 pad 67: /Drive_2/ENC_DATA0 -> /Drive_1/ENC_DIR4
- U2 pad 74: Net-(U2-Pad74) -> /Drive_2/ENC_DATA0
- U2 pad 75: Net-(U2-Pad75) -> /Drive_2/ENC_DIR0
- U2 pad 78: /Drive_1/ENC_DATA0 -> /Drive_2/ENC_DATA1
- U2 pad 79: /Drive_1/ENC_DIR0 -> /Drive_2/ENC_DIR1
- U2 pad 80: /Drive_1/ENC_DATA1 -> /Drive_2/ENC_DATA2
- U2 pad 81: /Drive_1/ENC_DIR1 -> /Drive_2/ENC_DIR2
- U2 pad 82: /Drive_1/ENC_DATA2 -> /Drive_2/ENC_DATA3
- U2 pad 83: /Drive_1/ENC_DIR2 -> /Drive_2/ENC_DIR3
- U2 pad 84: /Drive_1/ENC_DATA3 -> /Drive_2/ENC_DATA4
- U2 pad 85: /Drive_1/ENC_DIR3 -> /Drive_2/ENC_DIR4
- U2 pad 87: /Drive_1/ENC_DATA4 -> /FPGA/AUX_CLK
- U2 pad 88: /Drive_1/ENC_DIR4 -> /FPGA/AUX_DATA
- U2 pad 92: Net-(U2-Pad92) -> /FPGA/FAN
- U22 pad 26: +3V3 -> +3.3V
- U22 pad 27: +3V3 -> +3.3V
- U22 pad 28: +3V3 -> +3.3V
- U22 pad 3: +3V3 -> +3.3V
- U22 pad 33: (no net) -> GND
- U28 pad 10: +3V3 -> +3.3V
- U36 pad 10: +3V3 -> +3.3V
- U4 pad 2: /FPGA/TRXA0_N -> /FPGA/TRXA0_P
- U4 pad 3: /FPGA/TRXA0_P -> /FPGA/TRXA0_N
- U4 pad 49: (no net) -> GND
- U4 pad 5: /FPGA/TRXB0_N -> /FPGA/TRXB0_P
- U4 pad 6: /FPGA/TRXB0_P -> /FPGA/TRXB0_N
- U4 pad 7: /FPGA/TRXC0_N -> /FPGA/TRXC0_P
- U4 pad 8: /FPGA/TRXC0_P -> /FPGA/TRXC0_N
- U41 pad 4: +3V3 -> +3.3V
- U43 pad 10: +3V3 -> +3.3V
- U5 pad 1: +3V3 -> +3.3V
- U53 pad 10: +3V3 -> +3.3V
- U54 pad 10: +3V3 -> +3.3V
- U7 pad 49: (no net) -> GND
- U9 pad 10: +3V3 -> +3.3V
- X1 pad 5: /Drive_1/BRIDGE- -> /Drive_1/ISOL_15V
- X2 pad 5: /Drive_2/BRIDGE- -> /Drive_2/ISOL_15V
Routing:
- net GND: track 87.2 -> 304.6 mm, vias 7 -> 58
- net +5V: track 9.92 -> 142.0 mm, vias 0 -> 6
- net /Drive_1/VOLTAGE_CLOCK: track 0.00 -> 128.7 mm, vias 0 -> 3
- net /FPGA/VOLTAGE_D1: track 0.00 -> 125.8 mm, vias 0 -> 2
- net Net-(R134-Pad2): track 0.00 -> 111.1 mm
- net -5V: track 19.1 -> 127.2 mm, vias 0 -> 6
- net Net-(R133-Pad2): track 0.00 -> 107.1 mm
- net Net-(R131-Pad2): track 0.00 -> 106.4 mm
- net /FPGA/SCL: track 0.00 -> 105.7 mm, vias 0 -> 3
- net Net-(R132-Pad2): track 0.00 -> 104.5 mm
- net /FPGA/SDA: track 0.00 -> 104.1 mm, vias 0 -> 3
- net /FPGA/VOLTAGE_D0: track 0.00 -> 85.5 mm, vias 0 -> 2
- net /Drive_1/BRIDGE-: track 1.60 -> 79.3 mm, vias 0 -> 39
- net +12V: track 2.02 -> 78.8 mm, vias 0 -> 8
- net +3.3V: track 229.1 -> 301.9 mm, vias 13 -> 25
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- added copper zone on In2.Cu, net +12V
- added copper zone on In1.Cu, net /Drive_1/BRIDGE-
- added copper zone on In1.Cu, net /Drive_2/BRIDGE-
- added copper zone on In1.Cu, net GND
